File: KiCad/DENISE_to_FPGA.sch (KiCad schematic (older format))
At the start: 11 parts, among them J1 Conn_01x02, J3 Conn_01x01, U1 Denise_Socket, U2 Denise_MB_PinHeader, U3 LM1117-3.3

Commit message: New design, more routing done
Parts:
- removed BT1: Jumper_2_Open, Connector_PinHeader_2.54mm:PinHeader_1x02_P2.54mm_Horizontal, symbol Jumper:Jumper_2_Open
- removed J3: Conn_01x01, Connector_PinHeader_2.54mm:PinHeader_1x01_P2.54mm_Horizontal, symbol Connector_Generic:Conn_01x01
- removed U1: Denise_Socket, Package_DIP:DIP-48_W15.24mm_Socket_LongPads, symbol DENISE_to_FPGA:Denise
- added J2: Conn_01x40, Connector_FFC-FPC:Hirose_FH12-40S-0.5SH_1x40-1MP_P0.50mm_Horizontal, symbol Connector_Generic_MountingPin:Conn_01x40_MountingPin
- added U1, U2: 74LVC245A, Package_SO:TSSOP-20_4.4x6.5mm_P0.65mm, symbol DENISE_to_FPGA:74LVC245A
- U4: renamed from U2; footprint Package_DIP:DIP-48_W15.24mm_LongPads -> DENISE_to_FPGA:DIP-48_W15.24mm_Socket_LongPads
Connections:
- net labels added: C7M_3V3, CDAC_3V3, PIXELSW_3V3
- wire segments 24 -> 48
- no-connect marks 0 -> 3
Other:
- moved on the sheet: U4

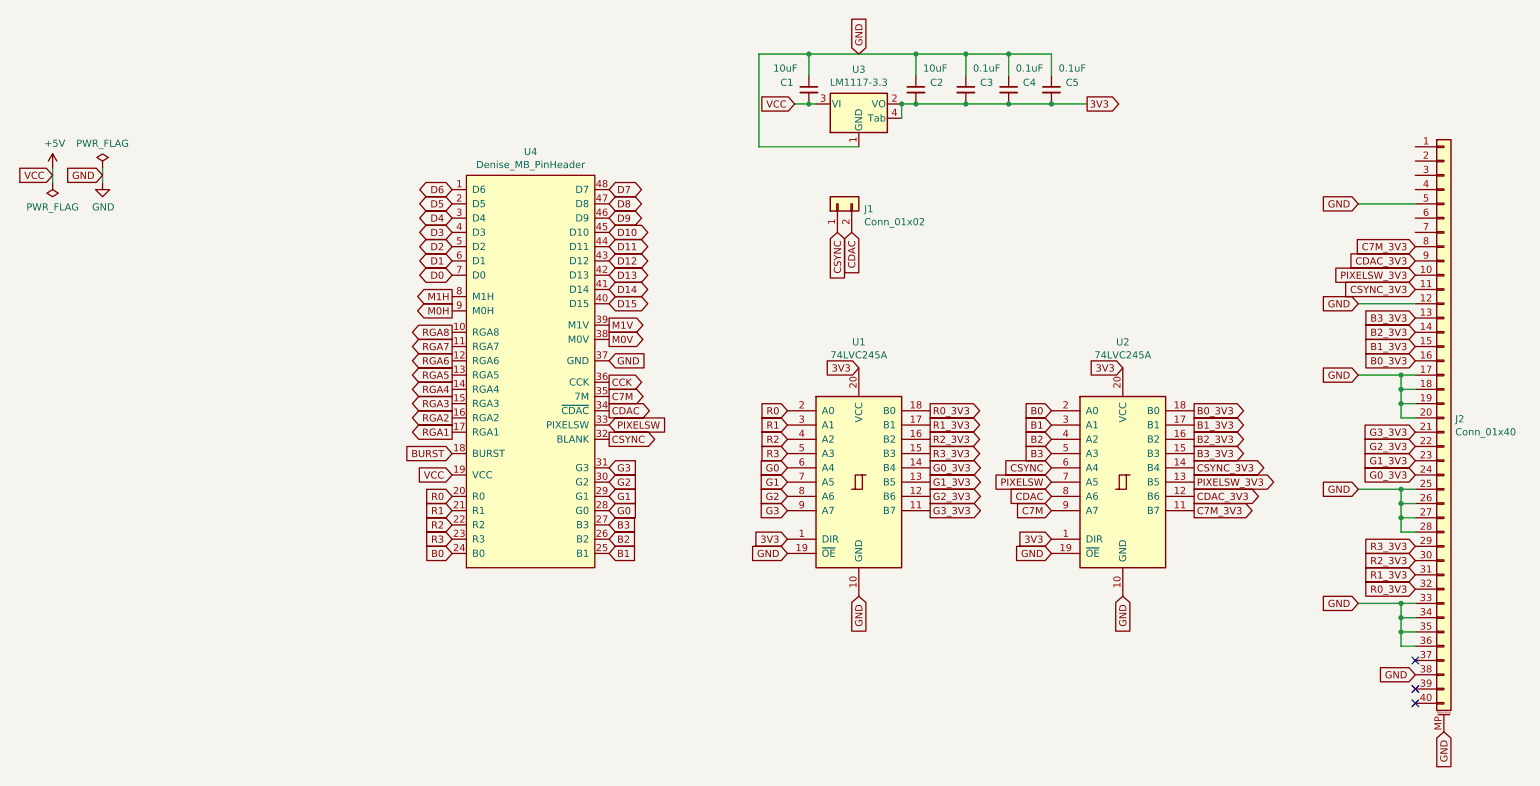
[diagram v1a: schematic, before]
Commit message: Added a 74LVC1G86 XOR gate and modified the 40-pin FPC to also take a TE Connectivity 4-1734592-0, and added Hsync,Vsync-header
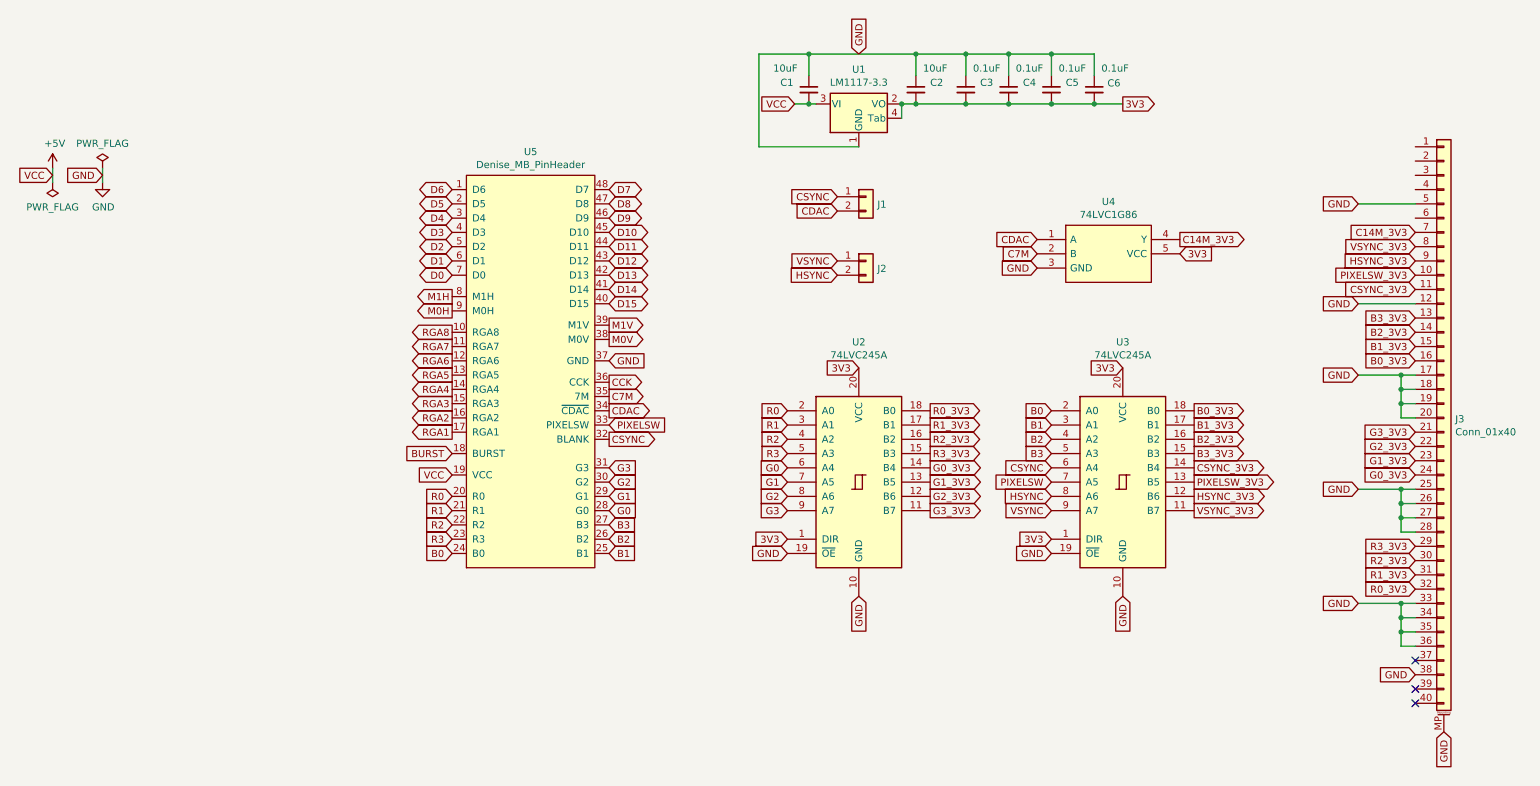
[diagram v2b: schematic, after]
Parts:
- added C6: 0.1uF, Capacitor_SMD:C_0805_2012Metric_Pad1.18x1.45mm_HandSolder, symbol Device:C_Small
- added J2: Conn_01x02, Connector_PinHeader_2.54mm:PinHeader_1x02_P2.54mm_Horizontal, symbol Connector_Generic:Conn_01x02
- added U4: 74LVC1G86, Package_TO_SOT_SMD:SOT-353_SC-70-5_Handsoldering, symbol DENISE_to_FPGA:74LVC1G86
- renumbered J2 to J3, U3 to U1, U1 to U2, U2 to U3, U4 to U5
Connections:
- net 3V3: now also C6.2, U4.5 (VCC)
- net C7M: now also U4.2 (B); no longer U3.9 (A7)
- net CDAC: now also U4.1 (A); no longer U3.8 (A6)
- net GND: now also C6.1, U4.3 (GND)
- net C14M_3V3: now reaches J3.7 (Pin_7)
- net C14M_3V3: now also U4.4 (Y)
- net C7M_3V3 renamed VSYNC_3V3
- net CDAC_3V3 renamed HSYNC_3V3
- new net HSYNC: J2.2 (Pin_2), U3.8 (A6)
- new net VSYNC: J2.1 (Pin_1), U3.9 (A7)
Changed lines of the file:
@@
 $EndDescr
 $Comp
-L power:PWR_FLAG #FLG0101
+L power:PWR_FLAG #FLG01
 U 1 1 62293CD1
 P 900 1750
-F 0 "#FLG0101" H 900 1825 50  0001 C CNN
+F 0 "#FLG01" H 900 1825 50  0001 C CNN
 F 1 "PWR_FLAG" H 900 1923 50  0000 C CNN
 F 2 "" H 900 1750 50  0001 C CNN
@@
 $EndComp
 $Comp
-L power:+5V #PWR0101
+L power:+5V #PWR01
 U 1 1 622948A4
 P 900 1650
-F 0 "#PWR0101" H 900 1500 50  0001 C CNN
+F 0 "#PWR01" H 900 1500 50  0001 C CNN
 F 1 "+5V" H 915 1823 50  0000 C CNN
 F 2 "" H 900 1650 50  0001 C CNN
@@
 VCC
 $Comp
-L power:PWR_FLAG #FLG0102
+L power:PWR_FLAG #FLG02
 U 1 1 622956B5
 P 1250 1650
-F 0 "#FLG0102" H 1250 1725 50  0001 C CNN
+F 0 "#FLG02" H 1250 1725 50  0001 C CNN
 F 1 "PWR_FLAG" H 1250 1823 50  0000 C CNN
 F 2 "" H 1250 1650 50  0001 C CNN
@@
 $EndComp
 $Comp
-L power:GND #PWR0102
+L power:GND #PWR02
 U 1 1 62295B6C
 P 1250 1750
-F 0 "#PWR0102" H 1250 1500 50  0001 C CNN
+F 0 "#PWR02" H 1250 1500 50  0001 C CNN
 F 1 "GND" H 1255 1577 50  0000 C CNN
 F 2 "" H 1250 1750 50  0001 C CNN
@@
 GND
 $Comp
-L DENISE_to_FPGA:Denise U4
+L DENISE_to_FPGA:Denise U5
 U 1 1 623BE5C5
 P 4250 3100
-F 0 "U4" H 4250 4665 50  0000 C CNN
+F 0 "U5" H 4250 4665 50  0000 C CNN
 F 1 "Denise_MB_PinHeader" H 4250 4574 50  0000 C CNN
 F 2 "DENISE_to_FPGA:DIP-48_W15.24mm_Socket_LongPads" H 4200 1600 50  0001 C CNN
@@
 Text GLabel 8900 3450 2    50   Output ~ 0
 B1_3V3
-Text GLabel 6400 2100 3    50   Input ~ 0
+Text GLabel 6400 1850 0    50   Input ~ 0
 CSYNC
 Text GLabel 8900 3650 2    50   Output ~ 0
@@
 R3_3V3
 $Comp
-L DENISE_to_FPGA:LM1117-3.3 U3
+L DENISE_to_FPGA:LM1117-3.3 U1
 U 1 1 6246B1F1
 P 6550 1200
-F 0 "U3" H 6550 1442 50  0000 C CNN
+F 0 "U1" H 6550 1442 50  0000 C CNN
 F 1 "LM1117-3.3" H 6550 1351 50  0000 C CNN
 F 2 "Package_TO_SOT_SMD:SOT-223" H 6550 1200 50  0001 C CNN
@@
 	6850 1200 6950 1200
 Connection ~ 6850 1200
-Text GLabel 8150 1200 2    50   Output ~ 0
+Text GLabel 8400 1200 2    50   Output ~ 0
 3V3
 $Comp
@@
 	7900 850  7600 850
 Connection ~ 7600 850
-Wire Wire Line
-	7900 1200 8150 1200
-Connection ~ 7900 1200
-$Comp
-L Connector_Generic:Conn_01x02 J1
-U 1 1 64E5B9C7
-P 6400 1900
-F 0 "J1" V 6364 1712 50  0000 R CNN
-F 1 "Conn_01x02" V 6273 1712 50  0000 R CNN
-F 2 "Connector_PinHeader_2.54mm:PinHeader_1x02_P2.54mm_Horizontal" H 6400 1900 50  0001 C CNN
-F 3 "~" H 6400 1900 50  0001 C CNN
-	1    6400 1900
-	0    -1   -1   0
-$EndComp
-Text GLabel 6500 2100 3    50   Input ~ 0
+Text GLabel 6400 1950 0    50   Input ~ 0
 CDAC
 $Comp
-L DENISE_to_FPGA:74LVC245A U1
+L DENISE_to_FPGA:74LVC245A U2
 U 1 1 64E6F2EB
 P 6550 3850
-F 0 "U1" H 6550 4831 50  0000 C CNN
+F 0 "U2" H 6550 4831 50  0000 C CNN
 F 1 "74LVC245A" H 6550 4740 50  0000 C CNN
 F 2 "Package_SO:TSSOP-20_4.4x6.5mm_P0.65mm" H 6550 3850 50  0001 C CNN
@@
 $EndComp
 $Comp
-L DENISE_to_FPGA:74LVC245A U2
+L DENISE_to_FPGA:74LVC245A U3
 U 1 1 64E71AF2
 P 8400 3850
-F 0 "U2" H 8400 4831 50  0000 C CNN
+F 0 "U3" H 8400 4831 50  0000 C CNN
 F 1 "74LVC245A" H 8400 4740 50  0000 C CNN
 F 2 "Package_SO:TSSOP-20_4.4x6.5mm_P0.65mm" H 8400 3850 50  0001 C CNN
@@
 GND
 $Comp
-L Connector_Generic_MountingPin:Conn_01x40_MountingPin J2
+L Connector_Generic_MountingPin:Conn_01x40_MountingPin J3
 U 1 1 64E8ADCA
 P 10650 3400
-F 0 "J2" H 10730 3392 50  0000 L CNN
+F 0 "J3" H 10730 3392 50  0000 L CNN
 F 1 "Conn_01x40" H 10730 3301 50  0000 L CNN
 F 2 "Connector_FFC-FPC:Hirose_FH12-40S-0.5SH_1x40-1MP_P0.50mm_Horizontal" H 10650 3400 50  0001 C CNN
@@
 Text GLabel 7900 3850 0    50   Input ~ 0
 PIXELSW
-Text GLabel 7900 3950 0    50   Input ~ 0
+Text GLabel 7800 2150 0    50   Input ~ 0
 CDAC
-Text GLabel 7900 4050 0    50   Input ~ 0
+Text GLabel 7800 2250 0    50   Input ~ 0
 C7M
 Text GLabel 8900 3850 2    50   Output ~ 0
 PIXELSW_3V3
-Text GLabel 8900 3950 2    50   Output ~ 0
-CDAC_3V3
-Text GLabel 8900 4050 2    50   Output ~ 0
-C7M_3V3
+Text GLabel 8800 2150 2    50   Output ~ 0
+C14M_3V3
 Text GLabel 10450 3500 0    50   Input ~ 0
 G3_3V3
@@
 Text GLabel 10450 2400 0    50   Input ~ 0
 PIXELSW_3V3
-Text GLabel 10450 2300 0    50   Input ~ 0
-CDAC_3V3
-Text GLabel 10450 2200 0    50   Input ~ 0
-C7M_3V3
 Text GLabel 10050 1900 0    50   Input ~ 0
 GND
@@
 Text GLabel 10650 5600 3    50   Input ~ 0
 GND
+Text GLabel 7900 3950 0    50   Input ~ 0
+HSYNC
+Text GLabel 8900 3950 2    50   Output ~ 0
+HSYNC_3V3
+Text GLabel 10450 2300 0    50   Input ~ 0
+HSYNC_3V3
+Text GLabel 7900 4050 0    50   Input ~ 0
+VSYNC
+Text GLabel 8900 4050 2    50   Output ~ 0
+VSYNC_3V3
+Text GLabel 10450 2200 0    50   Input ~ 0
+VSYNC_3V3
+Text GLabel 6400 2400 0    50   Input ~ 0
+HSYNC
+Text GLabel 6400 2300 0    50   Input ~ 0
+VSYNC
+Text GLabel 10450 2100 0    50   Input ~ 0
+C14M_3V3
+$Comp
+L DENISE_to_FPGA:74LVC1G86 U4
+U 1 1 64FB8746
+P 8300 2250
+F 0 "U4" H 8300 2615 50  0000 C CNN
+F 1 "74LVC1G86" H 8300 2524 50  0000 C CNN
+F 2 "Package_TO_SOT_SMD:SOT-353_SC-70-5_Handsoldering" H 8650 2450 50  0001 L CNN
+F 3 "" H 8650 2350 50  0001 L CNN
+	1    8300 2250
+	1    0    0    -1
+$EndComp
+Text GLabel 7800 2350 0    50   Input ~ 0
+GND
+Text GLabel 8800 2250 2    50   Input ~ 0
+3V3
+$Comp
+L Connector_Generic:Conn_01x02 J1
+U 1 1 64FC8747
+P 6600 1850
+F 0 "J1" H 6680 1796 50  0000 L CNN
+F 1 "Conn_01x02" H 6680 1751 50  0001 L CNN
+F 2 "Connector_PinHeader_2.54mm:PinHeader_1x02_P2.54mm_Horizontal" H 6600 1850 50  0001 C CNN
+F 3 "~" H 6600 1850 50  0001 C CNN
+	1    6600 1850
+	1    0    0    -1
+$EndComp
+Wire Wire Line
+	7900 1200 8200 1200
+Connection ~ 7900 1200
+$Comp
+L Connector_Generic:Conn_01x02 J2
+U 1 1 64FF4A26
+P 6600 2300
+F 0 "J2" H 6680 2246 50  0000 L CNN
+F 1 "Conn_01x02" H 6680 2201 50  0001 L CNN
+F 2 "Connector_PinHeader_2.54mm:PinHeader_1x02_P2.54mm_Horizontal" H 6600 2300 50  0001 C CNN
+F 3 "~" H 6600 2300 50  0001 C CNN
+	1    6600 2300
+	1    0    0    -1
+$EndComp
+$Comp
+L Device:C_Small C6
+U 1 1 64F7D283
+P 8200 1100
+F 0 "C6" H 8292 1146 50  0000 L CNN
+F 1 "0.1uF" H 8250 1250 50  0000 L CNN
+F 2 "Capacitor_SMD:C_0805_2012Metric_Pad1.18x1.45mm_HandSolder" H 8200 1100 50  0001 C CNN
+F 3 "~" H 8200 1100 50  0001 C CNN
+	1    8200 1100
+	1    0    0    -1
+$EndComp
+Wire Wire Line
+	8200 1000 8200 850
+Wire Wire Line
+	8200 850  7900 850
+Connection ~ 7900 850
+Wire Wire Line
+	8200 1200 8400 1200
+Connection ~ 8200 1200
 $EndSCHEMATC

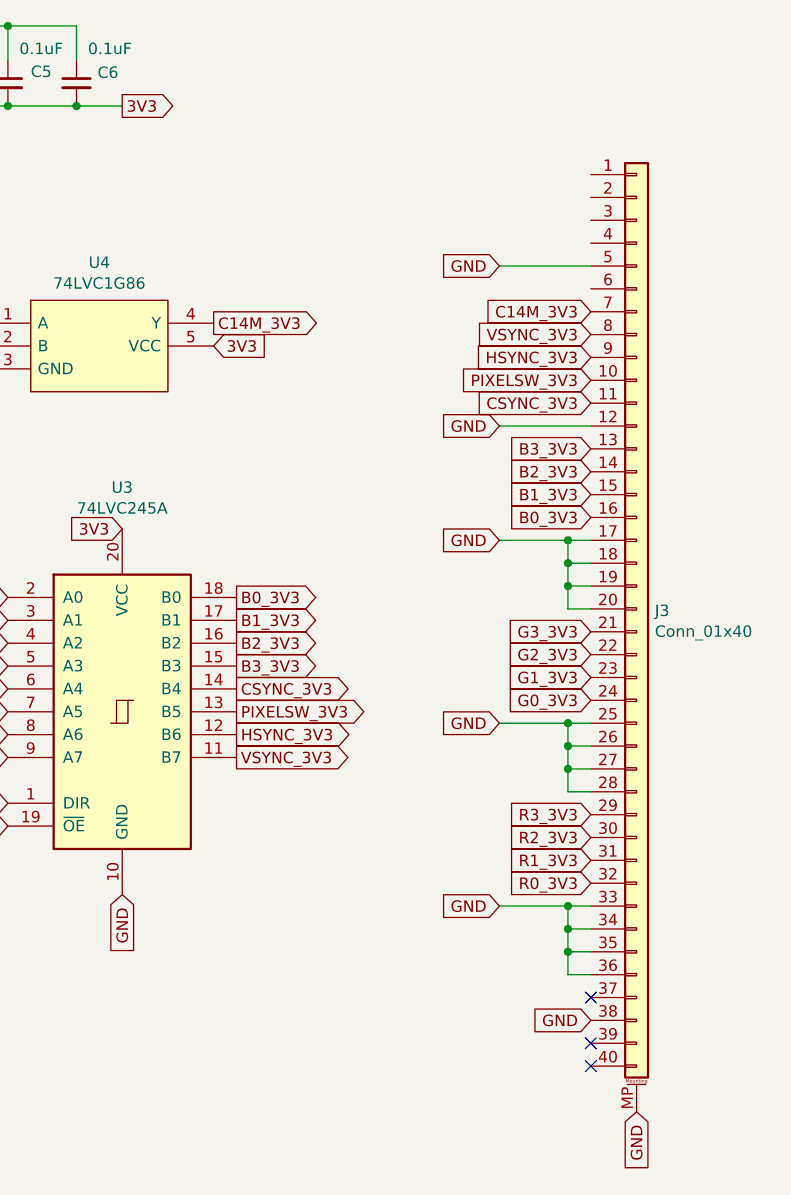
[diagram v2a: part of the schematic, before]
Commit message: Added a series resistor for C14M and changed some pin-assignments on the 40-pin FPC
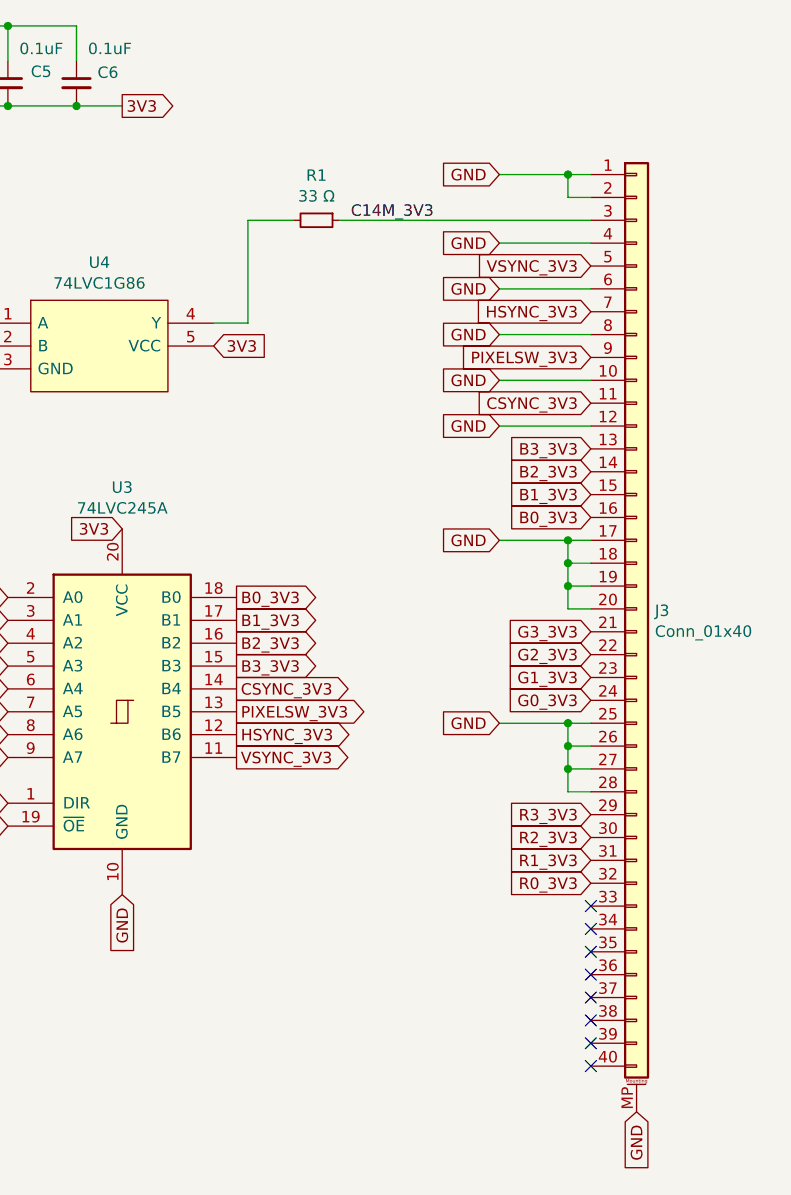
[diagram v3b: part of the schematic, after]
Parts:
- added R1: 33 Ω, Resistor_SMD:R_0805_2012Metric_Pad1.20x1.40mm_HandSolder, symbol Device:R_Small
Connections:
- net C14M_3V3: now also J3.3 (Pin_3), R1.1; no longer J3.7 (Pin_7), U4.4 (Y)
- net GND: now also J3.1 (Pin_1), J3.10 (Pin_10), J3.2 (Pin_2), J3.4 (Pin_4), J3.6 (Pin_6), J3.8 (Pin_8); no longer J3.33 (Pin_33), J3.34 (Pin_34), J3.35 (Pin_35), J3.36 (Pin_36), J3.38 (Pin_38), J3.5 (Pin_5)
- net HSYNC_3V3: now also J3.7 (Pin_7); no longer J3.9 (Pin_9)
- net PIXELSW_3V3: now also J3.9 (Pin_9); no longer J3.10 (Pin_10)
- net VSYNC_3V3: now also J3.5 (Pin_5); no longer J3.8 (Pin_8)
- new net: R1.2, U4.4 (Y)
- no-connect marks 3 -> 8
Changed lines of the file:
@@
 	1    0    0    -1
 $EndComp
-Text GLabel 10450 5200 0    50   Input ~ 0
-GND
 Text GLabel 10050 2600 0    50   Input ~ 0
 GND
@@
 Wire Wire Line
 	10450 3400 10350 3400
-Text GLabel 10050 4700 0    50   Input ~ 0
-GND
-Wire Wire Line
-	10450 4700 10350 4700
-Wire Wire Line
-	10350 4700 10350 4800
-Wire Wire Line
-	10350 4800 10450 4800
-Connection ~ 10350 4700
-Wire Wire Line
-	10350 4800 10350 4900
-Wire Wire Line
-	10350 4900 10450 4900
-Connection ~ 10350 4800
-Wire Wire Line
-	10350 4900 10350 5000
-Connection ~ 10350 4900
-Wire Wire Line
-	10050 4700 10350 4700
-Wire Wire Line
-	10450 5000 10350 5000
 Text GLabel 10050 3900 0    50   Input ~ 0
 GND
@@
 Wire Wire Line
 	10450 4200 10350 4200
-NoConn ~ 10450 5100
-NoConn ~ 10450 5300
-NoConn ~ 10450 5400
 Text GLabel 10450 3000 0    50   Input ~ 0
 B0_3V3
@@
 Text GLabel 8900 3850 2    50   Output ~ 0
 PIXELSW_3V3
-Text GLabel 8800 2150 2    50   Output ~ 0
-C14M_3V3
 Text GLabel 10450 3500 0    50   Input ~ 0
 G3_3V3
@@
 Text GLabel 10450 2500 0    50   Input ~ 0
 CSYNC_3V3
-Text GLabel 10450 2400 0    50   Input ~ 0
+Text GLabel 10450 2300 0    50   Input ~ 0
 PIXELSW_3V3
-Text GLabel 10050 1900 0    50   Input ~ 0
-GND
-Wire Wire Line
-	10050 1900 10450 1900
+Text GLabel 10050 2000 0    50   Input ~ 0
+GND
+Wire Wire Line
+	10050 2000 10450 2000
 Text GLabel 10650 5600 3    50   Input ~ 0
 GND
@@
 Text GLabel 8900 3950 2    50   Output ~ 0
 HSYNC_3V3
-Text GLabel 10450 2300 0    50   Input ~ 0
+Text GLabel 10450 2100 0    50   Input ~ 0
 HSYNC_3V3
 Text GLabel 7900 4050 0    50   Input ~ 0
@@
 Text GLabel 8900 4050 2    50   Output ~ 0
 VSYNC_3V3
-Text GLabel 10450 2200 0    50   Input ~ 0
+Text GLabel 10450 1900 0    50   Input ~ 0
 VSYNC_3V3
 Text GLabel 6400 2400 0    50   Input ~ 0
@@
 Text GLabel 6400 2300 0    50   Input ~ 0
 VSYNC
-Text GLabel 10450 2100 0    50   Input ~ 0
-C14M_3V3
 $Comp
 L DENISE_to_FPGA:74LVC1G86 U4
@@
 	8200 1200 8400 1200
 Connection ~ 8200 1200
+Text GLabel 10050 2400 0    50   Input ~ 0
+GND
+Wire Wire Line
+	10050 2400 10450 2400
+Text GLabel 10050 2200 0    50   Input ~ 0
+GND
+Wire Wire Line
+	10050 2200 10450 2200
+Text GLabel 10050 1800 0    50   Input ~ 0
+GND
+Wire Wire Line
+	10050 1800 10450 1800
+Text GLabel 10050 1500 0    50   Input ~ 0
+GND
+Wire Wire Line
+	10450 1500 10350 1500
+$Comp
+L Device:R_Small R1
+U 1 1 64FE39F6
+P 9250 1700
+F 0 "R1" V 9054 1700 50  0000 C CNN
+F 1 "33 Ω" V 9145 1700 50  0000 C CNN
+F 2 "Resistor_SMD:R_0805_2012Metric_Pad1.20x1.40mm_HandSolder" H 9250 1700 50  0001 C CNN
+F 3 "~" H 9250 1700 50  0001 C CNN
+	1    9250 1700
+	0    1    1    0
+$EndComp
+Wire Wire Line
+	8800 2150 8950 2150
+Wire Wire Line
+	8950 2150 8950 1700
+Wire Wire Line
+	8950 1700 9150 1700
+Wire Wire Line
+	9350 1700 10450 1700
+Text Label 9400 1700 0    50   ~ 0
+C14M_3V3
+NoConn ~ 10450 5400
+NoConn ~ 10450 5200
+NoConn ~ 10450 5000
+NoConn ~ 10450 4800
+NoConn ~ 10450 4700
+NoConn ~ 10450 4900
+NoConn ~ 10450 5100
+NoConn ~ 10450 5300
+Wire Wire Line
+	10450 1600 10350 1600
+Wire Wire Line
+	10350 1600 10350 1500
+Connection ~ 10350 1500
+Wire Wire Line
+	10350 1500 10050 1500
 $EndSCHEMATC
